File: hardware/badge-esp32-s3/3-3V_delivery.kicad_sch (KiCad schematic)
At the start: 20 parts, among them Q4 HL2301A, Q7 AO3424, U5 TPS63061DSCR, U8 TLV75733PDBVR

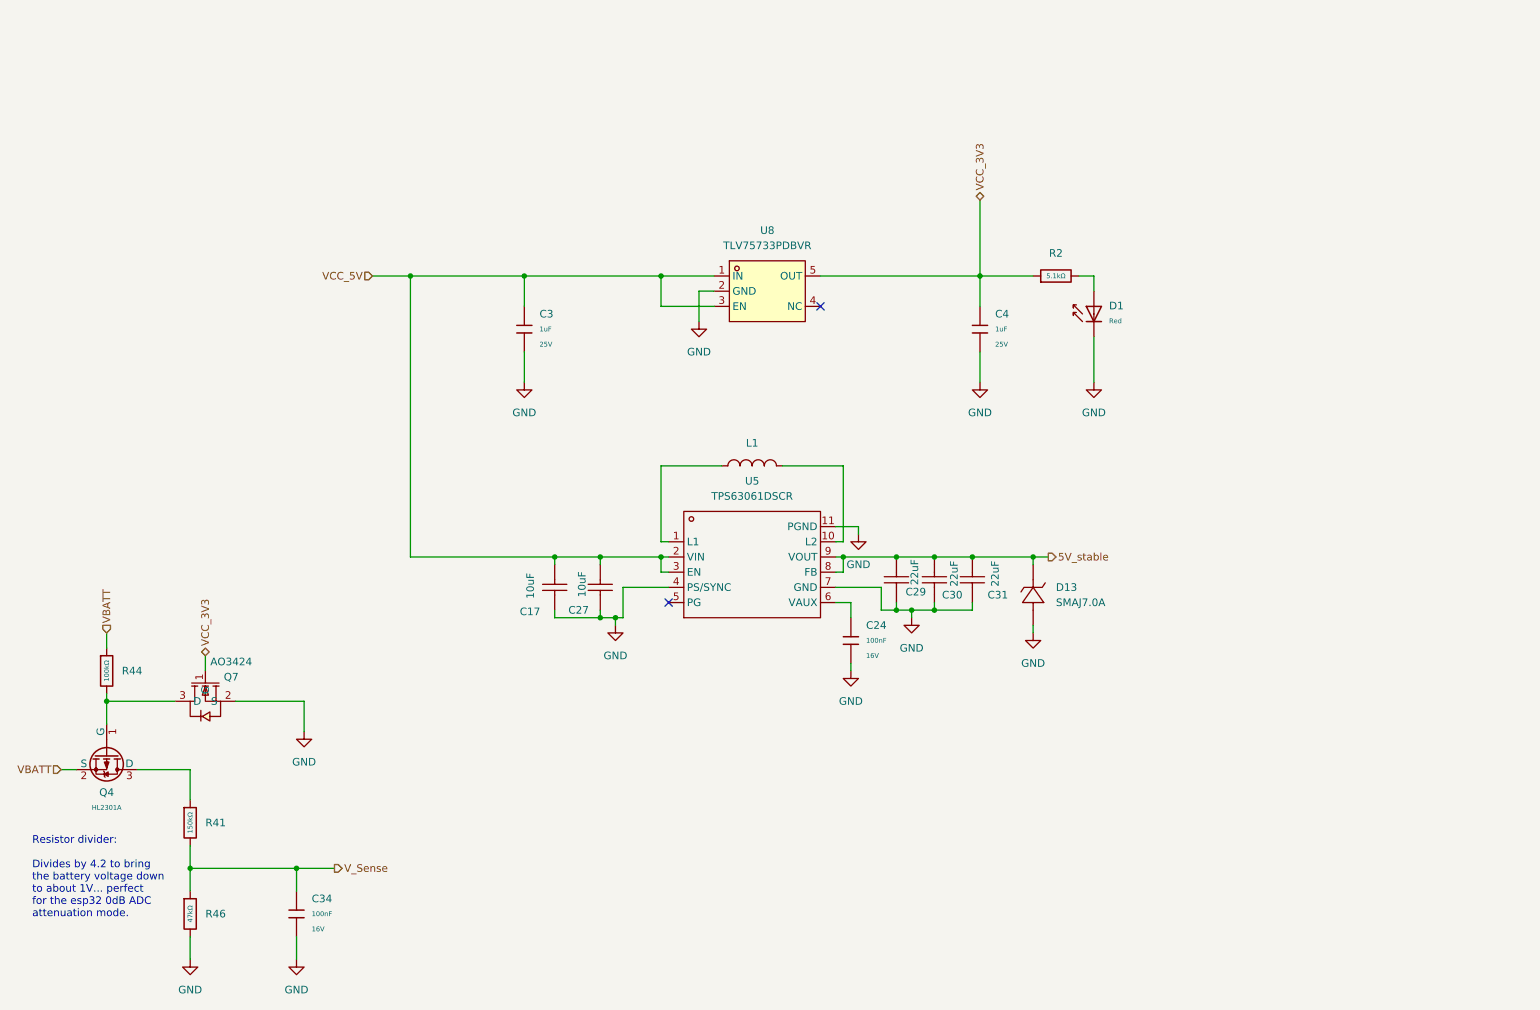
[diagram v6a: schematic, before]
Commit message: changed buck/boost reg and final touchups
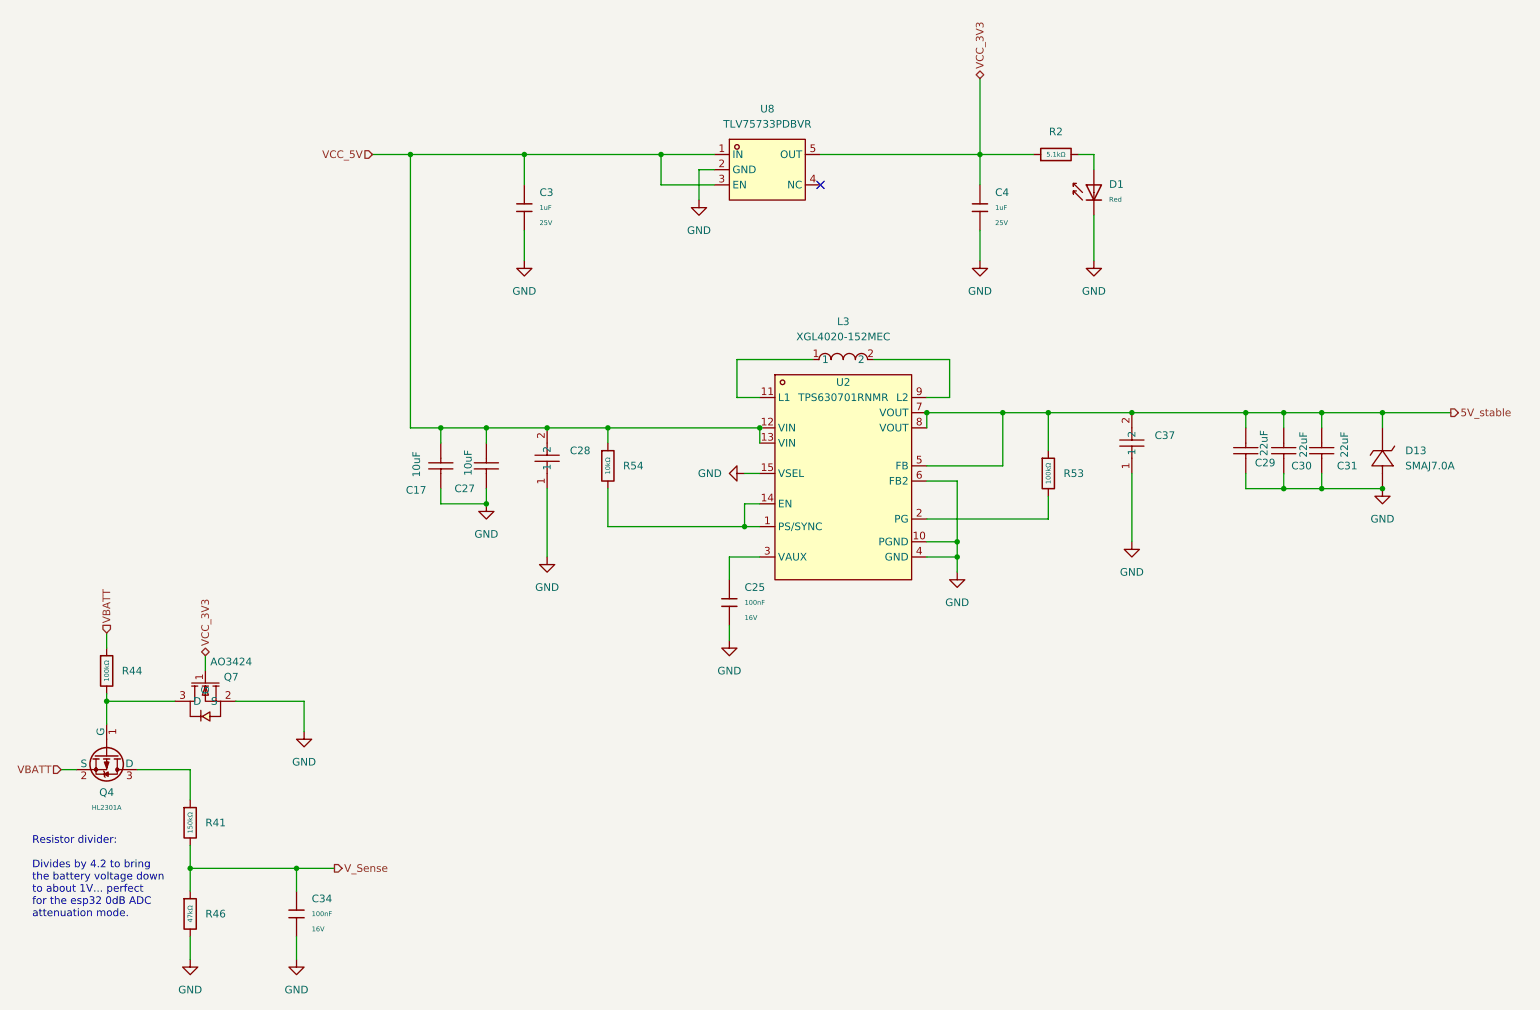
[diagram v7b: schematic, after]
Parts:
- removed C24: 100nF, PCM_JLCPCB:C_0402, symbol PCM_JLCPCB-Capacitors:0402,100nF
- removed L1: 1uH, lcsc-lib:IND-SMD_L4.0-W4.0_XFL4020-102MEB, symbol lcsc-lib:XFL4020-102MEC
- removed U5: TPS63061DSCR, lcsc-lib:WSON-10_L3.0-W3.0-P0.50-BL-EP-A, symbol lcsc-lib:TPS63061DSCR
- added C25: 100nF, PCM_JLCPCB:C_0402, symbol PCM_JLCPCB-Capacitors:0402,100nF
- added C28, C37: TMK107BBJ106MA-T, lcsc-lib:C0603, symbol lcsc-lib:TMK107BBJ106MA-T
- added L3: XGL4020-152MEC, lcsc-lib:IND-SMD_L4.0-W4.0_XEL4020, symbol lcsc-lib:XGL4020-152MEC
- added R53: 100kΩ, PCM_JLCPCB:R_0402, symbol PCM_JLCPCB-Resistors:0402,100kΩ
- added R54: 10kΩ, PCM_JLCPCB:R_0402, symbol PCM_JLCPCB-Resistors:0402,10kΩ
- added U2: TPS630701RNMR, lcsc-lib:VQFN-HR-15_L3.0-W2.5-P0.50-BL_TPS63070RNMR, symbol lcsc-lib:TPS630701RNMR
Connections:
- net 5V_stable: now also C37.2, R53.1, U2.5 (FB), U2.7 (VOUT), U2.8 (VOUT)
- net GND: now also C25.2, C28.1, C37.1, U2.10 (PGND), U2.15 (VSEL), U2.4 (GND), U2.6 (FB2)
- net VCC_5V: now also C28.2, R54.1, U2.12 (VIN), U2.13 (VIN)
- new net: R54.2, U2.1 (PS/SYNC), U2.14 (EN)
- new net: L3.1, U2.11 (L1)
- new net: R53.2, U2.2 (PG)
- new net: C25.1, U2.3 (VAUX)
- new net: L3.2, U2.9 (L2)
- no-connect marks 2 -> 1
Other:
- moved on the sheet: C17, C27, C29, C3, C30, C31, C4, D1, D13, R2, U8
